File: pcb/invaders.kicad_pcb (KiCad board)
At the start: 2 copper layers, 127 x 88.9 mm, 56 parts, among them J1 USB_B_Micro, J2 ISP, J3 Batt_In, SW1 Reset, SW10 SW_SPDT, SW2 D_Left, SW3 Trig_Left, SW4 D_Up, SW5 D_Down, SW6 D_Right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

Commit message: library fixes
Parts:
- renumbered D1 to OLED1, D2 to OLED2, D8 to OLED3
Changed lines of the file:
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@@
   )
   (setup
-    (last_trace_width 1.27)
+    (last_trace_width 0.2032)
     (user_trace_width 1.27)
     (trace_clearance 0.2032)
@@
       (effects (font (size 1 1) (thickness 0.15)) (justify mirror))
     )
-    (fp_line (start -3.3 3.05) (end -2 3.05) (layer B.SilkS) (width 0.12))
-    (fp_line (start -3.3 1.75) (end -3.3 3.05) (layer B.SilkS) (width 0.12))
-    (fp_line (start -1.9 2) (end -2.9 1) (layer B.Fab) (width 0.1))
-    (fp_line (start -3.25 -5.5) (end -3.25 3) (layer B.CrtYd) (width 0.05))
-    (fp_line (start -0.75 -5.5) (end -3.25 -5.5) (layer B.CrtYd) (width 0.05))
-    (fp_line (start -0.75 -13.75) (end -0.75 -5.5) (layer B.CrtYd) (width 0.05))
-    (fp_line (start 8.75 -13.75) (end -0.75 -13.75) (layer B.CrtYd) (width 0.05))
-    (fp_line (start 8.75 -5.5) (end 8.75 -13.75) (layer B.CrtYd) (width 0.05))
-    (fp_line (start 11.25 -5.5) (end 8.75 -5.5) (layer B.CrtYd) (width 0.05))
-    (fp_line (start 11.25 3) (end 11.25 -5.5) (layer B.CrtYd) (width 0.05))
-    (fp_line (start -3.25 3) (end 11.25 3) (layer B.CrtYd) (width 0.05))
-    (fp_line (start 8.95 -4.6) (end -0.95 -4.6) (layer B.SilkS) (width 0.12))
-    (fp_line (start -0.95 2.1) (end 8.95 2.1) (layer B.SilkS) (width 0.12))
-    (fp_line (start -3 -3.85) (end -3 1.35) (layer B.SilkS) (width 0.12))
-    (fp_line (start 11 1.35) (end 11 -3.85) (layer B.SilkS) (width 0.12))
+    (fp_line (start -1.9 2) (end 10.9 2) (layer B.Fab) (width 0.1))
+    (fp_line (start 10.9 2) (end 10.9 -4.5) (layer B.Fab) (width 0.1))
+    (fp_line (start 10.9 -4.5) (end -2.9 -4.5) (layer B.Fab) (width 0.1))
+    (fp_line (start -2.9 -4.5) (end -2.9 1) (layer B.Fab) (width 0.1))
+    (fp_line (start 4.5 -4.5) (end 4.5 -13.5) (layer B.Fab) (width 0.1))
+    (fp_line (start 4.5 -13.5) (end -0.5 -13.5) (layer B.Fab) (width 0.1))
+    (fp_line (start -0.5 -13.5) (end -0.5 -4.5) (layer B.Fab) (width 0.1))
     (fp_text user %R (at 4 -1.25 90) (layer B.Fab)
       (effects (font (size 1 1) (thickness 0.1)) (justify mirror))
     )
-    (fp_line (start -0.5 -13.5) (end -0.5 -4.5) (layer B.Fab) (width 0.1))
-    (fp_line (start 4.5 -13.5) (end -0.5 -13.5) (layer B.Fab) (width 0.1))
-    (fp_line (start 4.5 -4.5) (end 4.5 -13.5) (layer B.Fab) (width 0.1))
-    (fp_line (start -2.9 -4.5) (end -2.9 1) (layer B.Fab) (width 0.1))
-    (fp_line (start 10.9 -4.5) (end -2.9 -4.5) (layer B.Fab) (width 0.1))
-    (fp_line (start 10.9 2) (end 10.9 -4.5) (layer B.Fab) (width 0.1))
-    (fp_line (start -1.9 2) (end 10.9 2) (layer B.Fab) (width 0.1))
-    (pad "" thru_hole circle (at -2 1.75 90) (size 2 2) (drill 1.2) (layers *.Cu *.Mask))
-    (pad "" thru_hole circle (at 10 1.75 90) (size 2 2) (drill 1.2) (layers *.Cu *.Mask))
-    (pad "" thru_hole circle (at 10 -4.25 90) (size 2 2) (drill 1.2) (layers *.Cu *.Mask))
-    (pad "" thru_hole circle (at -2 -4.25 90) (size 2 2) (drill 1.2) (layers *.Cu *.Mask))
+    (fp_line (start 11 1.35) (end 11 -3.85) (layer B.SilkS) (width 0.12))
+    (fp_line (start -3 -3.85) (end -3 1.35) (layer B.SilkS) (width 0.12))
+    (fp_line (start -0.95 2.1) (end 8.95 2.1) (layer B.SilkS) (width 0.12))
+    (fp_line (start 8.95 -4.6) (end -0.95 -4.6) (layer B.SilkS) (width 0.12))
+    (fp_line (start -3.25 3) (end 11.25 3) (layer B.CrtYd) (width 0.05))
+    (fp_line (start 11.25 3) (end 11.25 -5.5) (layer B.CrtYd) (width 0.05))
+    (fp_line (start 11.25 -5.5) (end 8.75 -5.5) (layer B.CrtYd) (width 0.05))
+    (fp_line (start 8.75 -5.5) (end 8.75 -13.75) (layer B.CrtYd) (width 0.05))
+    (fp_line (start 8.75 -13.75) (end -0.75 -13.75) (layer B.CrtYd) (width 0.05))
+    (fp_line (start -0.75 -13.75) (end -0.75 -5.5) (layer B.CrtYd) (width 0.05))
+    (fp_line (start -0.75 -5.5) (end -3.25 -5.5) (layer B.CrtYd) (width 0.05))
+    (fp_line (start -3.25 -5.5) (end -3.25 3) (layer B.CrtYd) (width 0.05))
+    (fp_line (start -1.9 2) (end -2.9 1) (layer B.Fab) (width 0.1))
+    (fp_line (start -3.3 1.75) (end -3.3 3.05) (layer B.SilkS) (width 0.12))
+    (fp_line (start -3.3 3.05) (end -2 3.05) (layer B.SilkS) (width 0.12))
+    (pad 3 thru_hole circle (at 8 0 90) (size 1.7 1.7) (drill 0.9) (layers *.Cu *.Mask)
+      (net 3 +BATT))
+    (pad 2 thru_hole circle (at 4 0 90) (size 1.7 1.7) (drill 0.9) (layers *.Cu *.Mask)
+      (net 44 /BATT_IN))
     (pad 1 thru_hole circle (at 0 0 90) (size 1.7 1.7) (drill 0.9) (layers *.Cu *.Mask)
       (net 43 "Net-(SW10-Pad1)"))
-    (pad 2 thru_hole circle (at 4 0 90) (size 1.7 1.7) (drill 0.9) (layers *.Cu *.Mask)
-      (net 44 /BATT_IN))
-    (pad 3 thru_hole circle (at 8 0 90) (size 1.7 1.7) (drill 0.9) (layers *.Cu *.Mask)
-      (net 3 +BATT))
+    (pad "" thru_hole circle (at -2 -4.25 90) (size 2 2) (drill 1.2) (layers *.Cu *.Mask))
+    (pad "" thru_hole circle (at 10 -4.25 90) (size 2 2) (drill 1.2) (layers *.Cu *.Mask))
+    (pad "" thru_hole circle (at 10 1.75 90) (size 2 2) (drill 1.2) (layers *.Cu *.Mask))
+    (pad "" thru_hole circle (at -2 1.75 90) (size 2 2) (drill 1.2) (layers *.Cu *.Mask))
     (model ${KISYS3DMOD}/Button_Switch_THT.3dshapes/SW_E-Switch_EG1224_SPDT_Angled.wrl
       (at (xyz 0 0 0))
@@
   (module invaders:OLED_2in42_spi_i2c (layer F.Cu)
     (at 82.55 123.19)
-    (fp_text reference D2 (at -34.29 -8.89) (layer F.SilkS)
+    (fp_text reference OLED2 (at -34.29 -8.89) (layer F.SilkS)
       (effects (font (size 0.6477 0.6477) (thickness 0.1016)))
     )
@@
   (module invaders:OLED_1in5_spi_rgb (layer F.Cu)
     (at 82.55 124.46)
-    (fp_text reference D8 (at 0.092 15.88) (layer F.SilkS)
+    (fp_text reference OLED3 (at 0.092 15.88) (layer F.SilkS)
       (effects (font (size 0.6477 0.6477) (thickness 0.1016)))
     )
@@
     (descr "Through hole straight pin header, 1x04, 2.54mm pitch, single row")
     (tags "Through hole pin header THT 1x04 2.54mm single row")
-    (fp_text reference D1 (at 0 -3 270) (layer F.SilkS)
-      (effects (font (size 0.6477 0.6477) (thickness 0.1016)))
-    )
+    (fp_text reference OLED1 (at 0 -3 270) (layer F.SilkS)
+      (effects (font (size 0.6477 0.6477) (thickness 0.1016)))
+    )

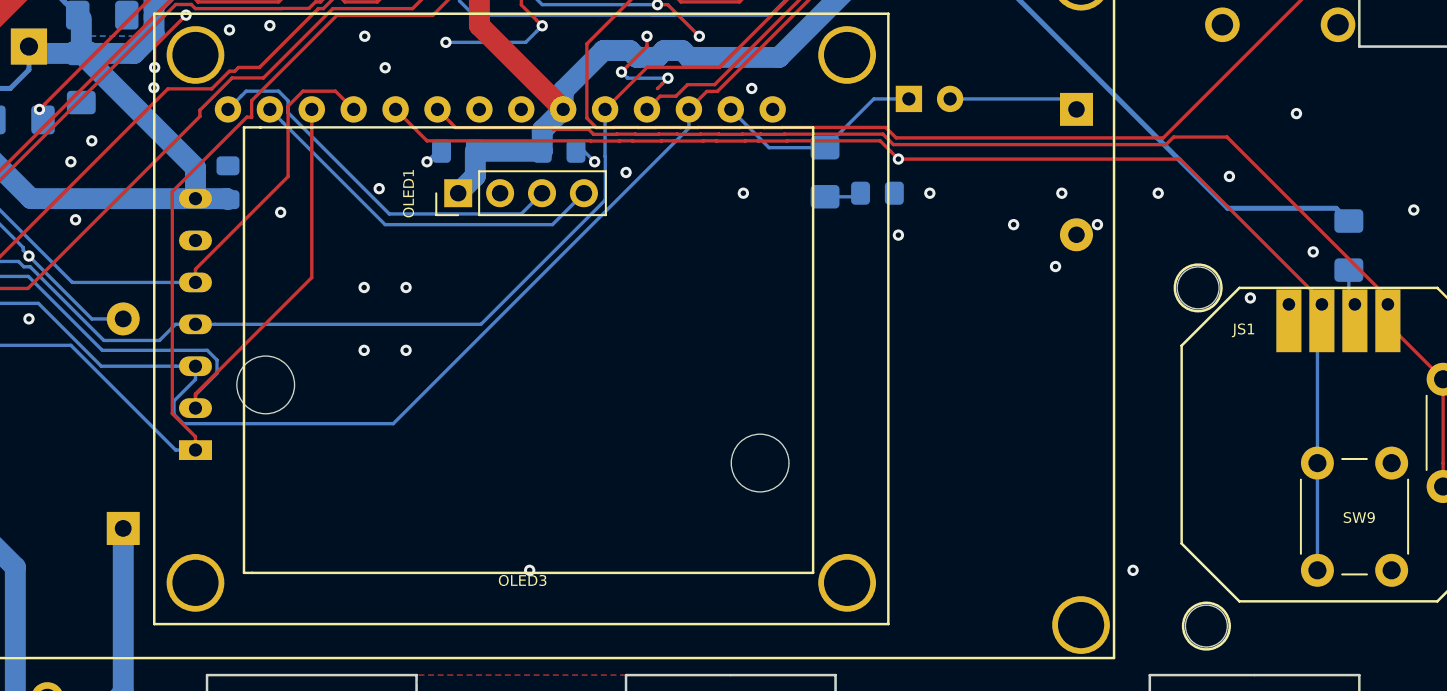
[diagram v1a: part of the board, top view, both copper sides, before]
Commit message: cleanup; add pullup to Panel_CS
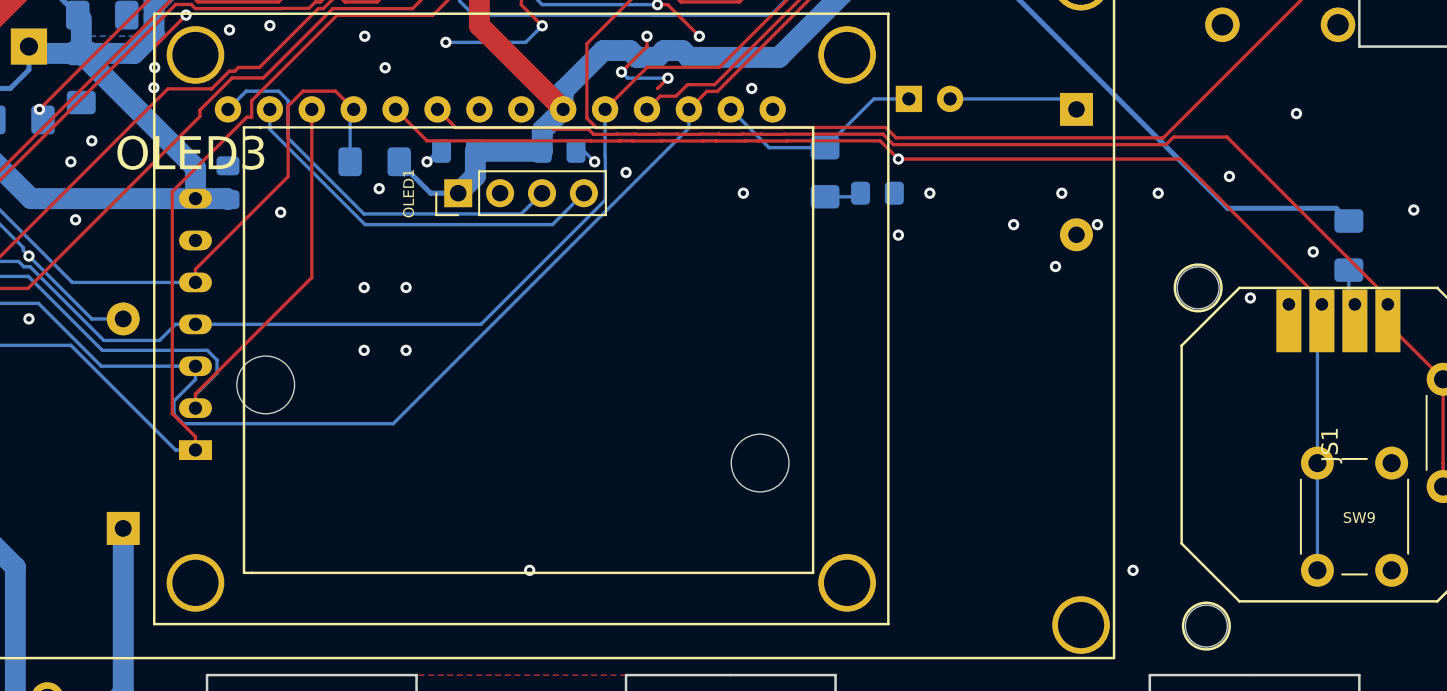
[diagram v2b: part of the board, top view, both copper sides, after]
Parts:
- added R9: 10k, Resistor_SMD:R_1206_3216Metric_Pad1.42x1.75mm_HandSolder, B.Cu at (73.7, 114.9)
- C10, C11: value 22p -> 22pF
- D3: value D_Schottky -> 0.35V
- D4: value 5V -> 5.1V
- JS1: value Micro_Thumb_JoyStick -> Thumbstick; footprint invaders:psp_thumbstick -> a-symbols:psp_thumbstick
- OLED1: footprint invaders:OLED_1in3_i2c -> a-symbols:OLED_1in3_i2c
- OLED2: footprint invaders:OLED_2in42_spi_i2c -> a-symbols:OLED_2in42_spi_i2c
- OLED3: footprint invaders:OLED_1in5_spi_rgb -> a-symbols:OLED_1in5_spi_rgb
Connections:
- J1 pad 2: Net-(J1-Pad2) -> (no net)
- J1 pad 3: Net-(J1-Pad3) -> (no net)
- J1 pad 4: Net-(J1-Pad4) -> (no net)
- SW10 pad 1: Net-(SW10-Pad1) -> (no net)
- U1 pad 15: /PWM1 -> (no net)
- U1 pad 21: Net-(U1-Pad21) -> (no net)
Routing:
- net +5V: track 214.2 -> 218.6 mm
- net /Panel_CS: track 34.5 -> 37.8 mm
- net /SCL: track 23.5 -> 24.4 mm
- net /SDA: track 22.7 -> 23.4 mm
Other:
- board text added: "ICSP"
- board text removed: "ISP"
